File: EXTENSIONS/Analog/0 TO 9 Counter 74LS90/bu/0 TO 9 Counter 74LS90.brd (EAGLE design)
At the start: 37 x 71 mm, 10 parts

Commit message: fix bug in pcb '0 TO 9 Counter 74LS90'
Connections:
- net BIT_3: now also SN74LS90N_1.14
- net SEG_1_DG: now also 74LS47N_0.14
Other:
- board text added: "PCBv2 - 2019.09"
- board text removed: "PCBv1 - 2019.08"
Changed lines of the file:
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@@
 <text x="34.5" y="17.7" size="0.8128" layer="25" rot="R180">OUT</text>
 <text x="34.5" y="15.2" size="0.8128" layer="25" rot="R180">OUT_R</text>
-<text x="19.5" y="17" size="1.27" layer="26" rot="MR0" align="center">PCBv1 - 2019.08</text>
+<text x="19.5" y="17" size="1.27" layer="26" rot="MR0" align="center">PCBv2 - 2019.09</text>
 <text x="35.5" y="43.4" size="2.25" layer="25" rot="R270" align="center">0 To 99 Counter</text>
 <text x="11.5" y="14.5" size="1.27" layer="25" rot="R180" align="center">INPUTS</text>
@@
 <contactref element="SN74LS90N_0" pad="11"/>
 <contactref element="74LS47N_0" pad="6"/>
-<wire x1="26.81" y1="27.5" x2="19.19" y2="45.69" width="0" layer="19" extent="1-1"/>
+<contactref element="SN74LS90N_1" pad="14"/>
+<wire x1="13.81" y1="35.12" x2="19.19" y2="45.69" width="0" layer="19" extent="1-1"/>
+<wire x1="26.81" y1="27.5" x2="13.81" y2="35.12" width="0" layer="19" extent="1-1"/>
 </signal>
 <signal name="N$1">
@@
 <signal name="SEG_1_DG">
 <contactref element="DIGIT_0_ANODE" pad="10"/>
+<contactref element="74LS47N_0" pad="14"/>
+<wire x1="26.81" y1="53.31" x2="18.92" y2="79.62" width="0" layer="19" extent="1-1"/>
 </signal>
 <signal name="N$2">

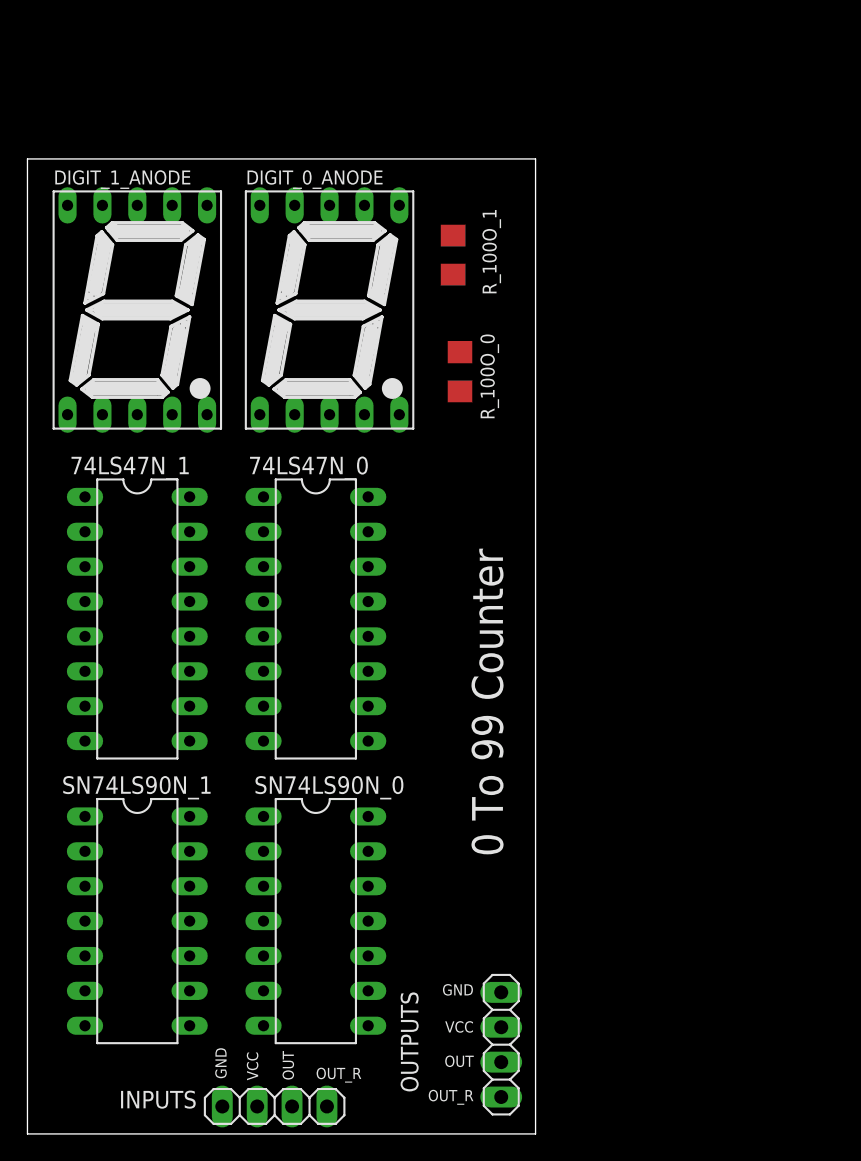
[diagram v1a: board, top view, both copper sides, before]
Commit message: Create v3 of 0 to 99 counter
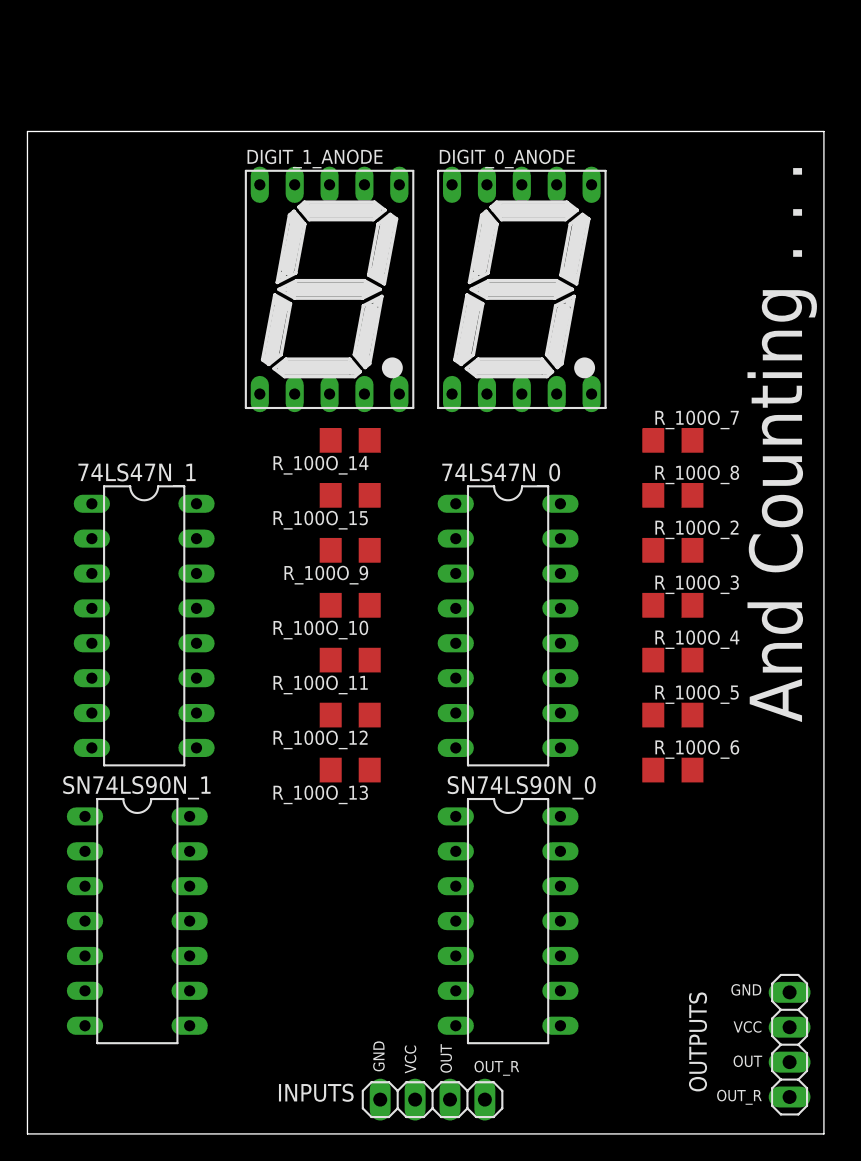
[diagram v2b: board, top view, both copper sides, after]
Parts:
- removed R_100O_0, R_100O_1: (no value), adafruit:R1206
- added R_100O_10, R_100O_11, R_100O_12, R_100O_13, R_100O_14, R_100O_15, R_100O_2, R_100O_3, R_100O_4, R_100O_5, R_100O_6, R_100O_7, R_100O_8, R_100O_9: (no value), adafruit:R1206
- moved OUTPUTS 21.0 mm to (57.5, 18.5)
- moved DIGIT_0_ANODE 14.1 mm to (38.0, 73.5)
- moved DIGIT_1_ANODE 14.1 mm to (24.0, 73.5)
- moved 74LS47N_0 14.0 mm to (37.0, 49.0)
- moved SN74LS90N_0 14.0 mm to (37.0, 27.5)
- moved JP_CLOCK_IN 11.5 mm to (31.5, 14.5)
- moved 74LS47N_1 0.71 mm to (10.5, 49.0)
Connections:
- removed net N$1: DIGIT_0_ANODE.8, R_100O_0.1
- removed net N$2: DIGIT_1_ANODE.8, R_100O_1.1
- new net SEG_1_DAA: DIGIT_0_ANODE.7, R_100O_2.2
- new net SEG_1_DBB: DIGIT_0_ANODE.6, R_100O_3.2
- new net SEG_1_DCC: DIGIT_0_ANODE.4, R_100O_4.2
- new net SEG_1_DDD: DIGIT_0_ANODE.2, R_100O_5.2
- new net SEG_1_DEE: DIGIT_0_ANODE.1, R_100O_6.2
- new net SEG_1_DFF: DIGIT_0_ANODE.9, R_100O_7.2
- new net SEG_1_DGG: DIGIT_0_ANODE.10, R_100O_8.2
- new net SEG_2_DAA: DIGIT_1_ANODE.7, R_100O_9.2
- new net SEG_2_DBB: DIGIT_1_ANODE.6, R_100O_10.2
- new net SEG_2_DCC: DIGIT_1_ANODE.4, R_100O_11.2
- new net SEG_2_DDD: DIGIT_1_ANODE.2, R_100O_12.2
- new net SEG_2_DEE: DIGIT_1_ANODE.1, R_100O_13.2
- new net SEG_2_DFF: DIGIT_1_ANODE.9, R_100O_14.2
- new net SEG_2_DGG: DIGIT_1_ANODE.10, R_100O_15.2
- net SEG_1_DA: now also R_100O_2.1; no longer DIGIT_0_ANODE.7
- net SEG_1_DB: now also R_100O_3.1; no longer DIGIT_0_ANODE.6
- net SEG_1_DC: now also R_100O_4.1; no longer DIGIT_0_ANODE.4
- net SEG_1_DD: now also R_100O_5.1; no longer DIGIT_0_ANODE.2
- net SEG_1_DE: now also R_100O_6.1; no longer DIGIT_0_ANODE.1
- net SEG_1_DF: now also R_100O_7.1; no longer DIGIT_0_ANODE.9
- net SEG_1_DG: now also R_100O_8.1; no longer DIGIT_0_ANODE.10
- net SEG_2_DA: now also R_100O_9.1; no longer DIGIT_1_ANODE.7
- net SEG_2_DB: now also R_100O_10.1; no longer DIGIT_1_ANODE.6
- net SEG_2_DC: now also R_100O_11.1; no longer DIGIT_1_ANODE.4
- net SEG_2_DD: now also R_100O_12.1; no longer DIGIT_1_ANODE.2
- net SEG_2_DE: now also R_100O_13.1; no longer DIGIT_1_ANODE.1
- net SEG_2_DF: now also R_100O_14.1; no longer DIGIT_1_ANODE.9
- net SEG_2_DG: now also R_100O_15.1; no longer DIGIT_1_ANODE.10
- net VCC: now also DIGIT_0_ANODE.8, DIGIT_1_ANODE.8; no longer R_100O_0.2, R_100O_1.2
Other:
- board size 37 x 71 mm -> 58 x 73 mm
- board text added: "And Counting . . ."
- board text added: "PCBv3 - 2019.12"
- board text removed: "0 To 99 Counter"
- board text removed: "PCBv2 - 2019.09"
